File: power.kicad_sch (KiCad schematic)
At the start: 11 parts

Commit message: Finished circuit
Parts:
- added J4: 5V, symbol Connector:Conn_01x10_Pin
- added J5: GND, symbol Connector:Conn_01x10_Pin
- gave numbers to parts that had none: 11
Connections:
- net +5V: now also J4.1 (Pin_1), J4.10 (Pin_10), J4.2 (Pin_2), J4.3 (Pin_3), J4.4 (Pin_4), J4.5 (Pin_5), J4.6 (Pin_6), J4.7 (Pin_7), J4.8 (Pin_8), J4.9 (Pin_9)
- net GND: now also J3.2, J5.1 (Pin_1), J5.10 (Pin_10), J5.2 (Pin_2), J5.3 (Pin_3), J5.4 (Pin_4), J5.5 (Pin_5), J5.6 (Pin_6), J5.7 (Pin_7), J5.8 (Pin_8), J5.9 (Pin_9)

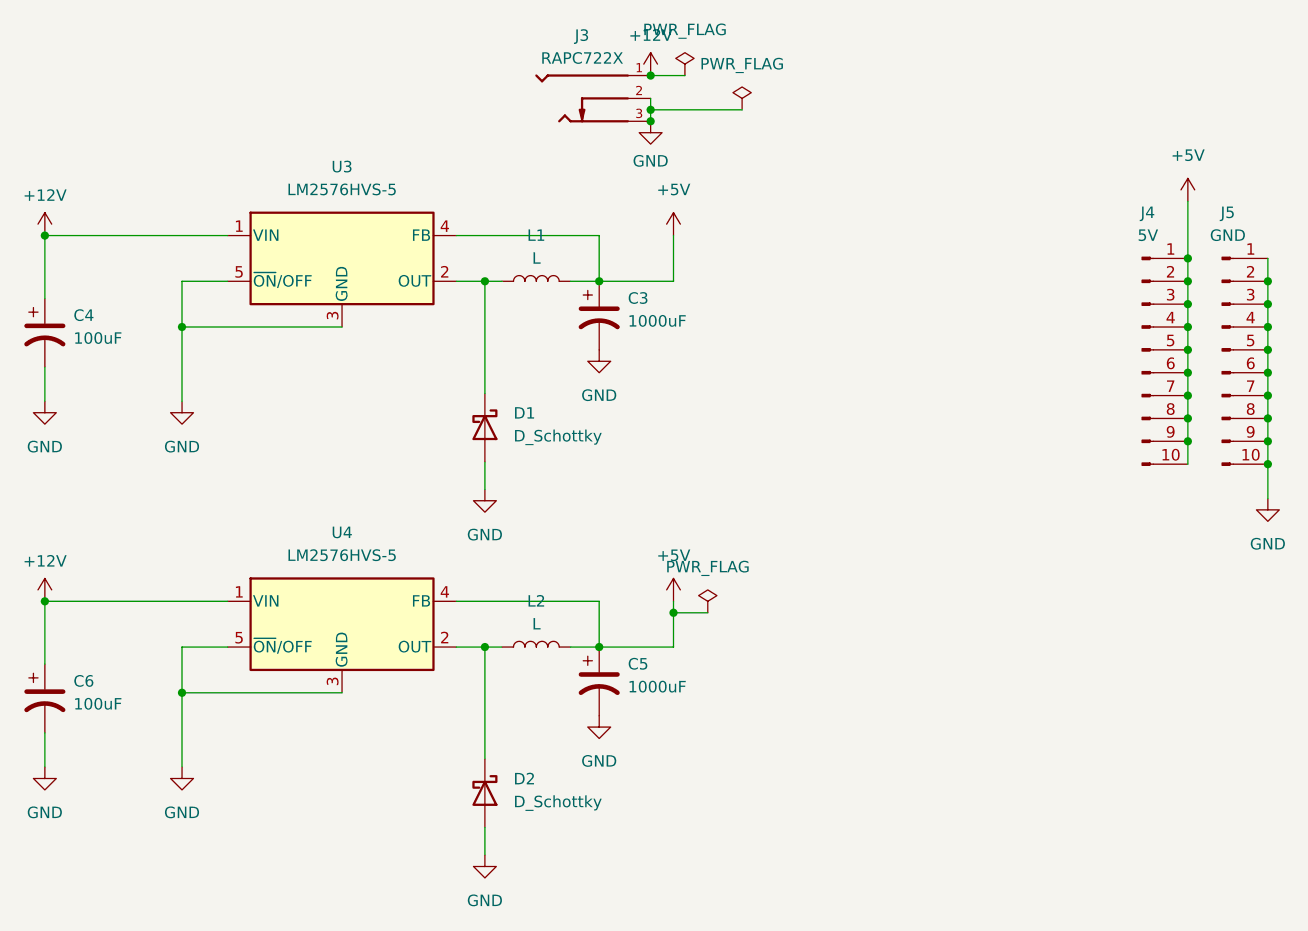
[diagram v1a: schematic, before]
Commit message: Updated the footprints for all the components.
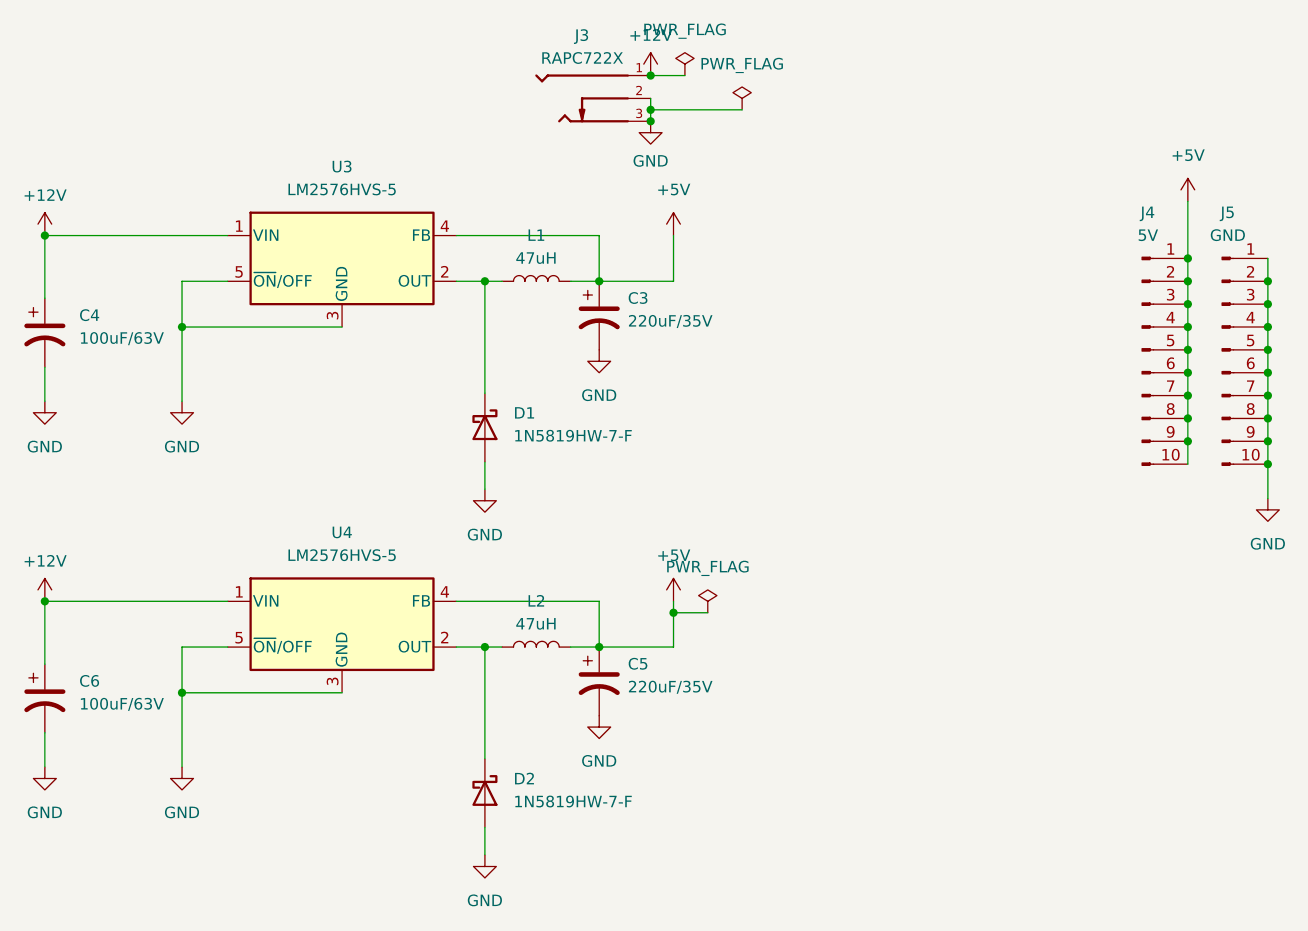
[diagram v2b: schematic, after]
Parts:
- C3, C5: value 1000uF -> 220uF/35V; footprint (none) -> Capacitor_SMD:CP_Elec_10x10; Field4 (none) -> EEH-ZA1V221P
- C4, C6: value 100uF -> 100uF/63V; footprint (none) -> Capacitor_SMD:CP_Elec_10x10; Field4 (none) -> UUX1J101MNL1GS
- D1, D2: value D_Schottky -> 1N5819HW-7-F; footprint (none) -> Diode_SMD:D_SOD-123
- J4, J5: footprint (none) -> Connector_PinSocket_2.54mm:PinSocket_2x05_P2.54mm_Vertical
- L1, L2: value L -> 47uH; footprint (none) -> Inductor_SMD:L_12x12mm_H8mm; Field4 (none) -> CDRH127/LDNP-470MC
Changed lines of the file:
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@@
       (effects (font (size 1.27 1.27)))
     )
-    (property "Value" "L" (at 82.55 90.17 90)
-      (effects (font (size 1.27 1.27)))
-    )
-    (property "Footprint" "" (at 82.55 92.71 0)
+    (property "Value" "47uH" (at 82.55 90.17 90)
+      (effects (font (size 1.27 1.27)))
+    )
+    (property "Footprint" "Inductor_SMD:L_12x12mm_H8mm" (at 82.55 92.71 0)
       (effects (font (size 1.27 1.27)) hide)
     )
     (property "Datasheet" "~" (at 82.55 92.71 0)
+      (effects (font (size 1.27 1.27)) hide)
+    )
+    (property "Field4" "CDRH127/LDNP-470MC" (at 82.55 92.71 90)
       (effects (font (size 1.27 1.27)) hide)
     )
@@
       (effects (font (size 1.27 1.27)))
     )
-    (property "Footprint" "" (at 158.75 59.69 0)
+    (property "Footprint" "Connector_PinSocket_2.54mm:PinSocket_2x05_P2.54mm_Vertical" (at 158.75 59.69 0)
       (effects (font (size 1.27 1.27)) hide)
     )
@@
       (effects (font (size 1.27 1.27)) (justify left))
     )
-    (property "Value" "D_Schottky" (at 80.01 69.2785 90)
-      (effects (font (size 1.27 1.27)) (justify left))
-    )
-    (property "Footprint" "" (at 76.835 68.326 0)
+    (property "Value" "1N5819HW-7-F" (at 80.01 69.2785 90)
+      (effects (font (size 1.27 1.27)) (justify left))
+    )
+    (property "Footprint" "Diode_SMD:D_SOD-123" (at 76.835 68.326 0)
       (effects (font (size 1.27 1.27)) hide)
     )
@@
   (symbol (lib_id "Device:C_Polarized_US") (at 27.94 98.425 0) (unit 1)
     (in_bom yes) (on_board yes) (dnp no) (fields_autoplaced)
-    (property "Reference" "C6" (at 31.115 96.52 0)
-      (effects (font (size 1.27 1.27)) (justify left))
-    )
-    (property "Value" "100uF" (at 31.115 99.06 0)
-      (effects (font (size 1.27 1.27)) (justify left))
-    )
-    (property "Footprint" "" (at 27.94 98.425 0)
+    (property "Reference" "C6" (at 31.75 96.52 0)
+      (effects (font (size 1.27 1.27)) (justify left))
+    )
+    (property "Value" "100uF/63V" (at 31.75 99.06 0)
+      (effects (font (size 1.27 1.27)) (justify left))
+    )
+    (property "Footprint" "Capacitor_SMD:CP_Elec_10x10" (at 27.94 98.425 0)
       (effects (font (size 1.27 1.27)) hide)
     )
@@
       (effects (font (size 1.27 1.27)) hide)
     )
+    (property "Field4" "UUX1J101MNL1GS" (at 27.94 98.425 0)
+      (effects (font (size 1.27 1.27)) hide)
+    )
     (pin "2")
     (pin "1")
@@
       (effects (font (size 1.27 1.27)) (justify left))
     )
-    (property "Value" "1000uF" (at 92.71 97.155 0)
-      (effects (font (size 1.27 1.27)) (justify left))
-    )
-    (property "Footprint" "" (at 89.535 96.52 0)
+    (property "Value" "220uF/35V" (at 92.71 97.155 0)
+      (effects (font (size 1.27 1.27)) (justify left))
+    )
+    (property "Footprint" "Capacitor_SMD:CP_Elec_10x10" (at 89.535 96.52 0)
       (effects (font (size 1.27 1.27)) hide)
     )
@@
       (effects (font (size 1.27 1.27)) hide)
     )
+    (property "Field4" "EEH-ZA1V221P" (at 89.535 96.52 0)
+      (effects (font (size 1.27 1.27)) hide)
+    )
     (pin "2")
     (pin "1")
@@
       (effects (font (size 1.27 1.27)))
     )
-    (property "Footprint" "" (at 149.86 59.69 0)
+    (property "Footprint" "Connector_PinSocket_2.54mm:PinSocket_2x05_P2.54mm_Vertical" (at 149.86 59.69 0)
       (effects (font (size 1.27 1.27)) hide)
     )
@@
       (effects (font (size 1.27 1.27)))
     )
-    (property "Value" "L" (at 82.55 49.53 90)
-      (effects (font (size 1.27 1.27)))
-    )
-    (property "Footprint" "" (at 82.55 52.07 0)
+    (property "Value" "47uH" (at 82.55 49.53 90)
+      (effects (font (size 1.27 1.27)))
+    )
+    (property "Footprint" "Inductor_SMD:L_12x12mm_H8mm" (at 82.55 52.07 0)
       (effects (font (size 1.27 1.27)) hide)
     )
@@
       (effects (font (size 1.27 1.27)) hide)
     )
+    (property "Field4" "CDRH127/LDNP-470MC" (at 82.55 52.07 90)
+      (effects (font (size 1.27 1.27)) hide)
+    )
     (pin "1")
     (pin "2")
@@
       (effects (font (size 1.27 1.27)) (justify left))
     )
-    (property "Value" "1000uF" (at 92.71 56.515 0)
-      (effects (font (size 1.27 1.27)) (justify left))
-    )
-    (property "Footprint" "" (at 89.535 55.88 0)
+    (property "Value" "220uF/35V" (at 92.71 56.515 0)
+      (effects (font (size 1.27 1.27)) (justify left))
+    )
+    (property "Footprint" "Capacitor_SMD:CP_Elec_10x10" (at 89.535 55.88 0)
       (effects (font (size 1.27 1.27)) hide)
     )
@@
       (effects (font (size 1.27 1.27)) hide)
     )
+    (property "Field4" "EEH-ZA1V221P" (at 89.535 55.88 0)
+      (effects (font (size 1.27 1.27)) hide)
+    )
     (pin "2")
     (pin "1")
@@
   (symbol (lib_id "Device:C_Polarized_US") (at 27.94 57.785 0) (unit 1)
     (in_bom yes) (on_board yes) (dnp no) (fields_autoplaced)
-    (property "Reference" "C4" (at 31.115 55.88 0)
-      (effects (font (size 1.27 1.27)) (justify left))
-    )
-    (property "Value" "100uF" (at 31.115 58.42 0)
-      (effects (font (size 1.27 1.27)) (justify left))
-    )
-    (property "Footprint" "" (at 27.94 57.785 0)
+    (property "Reference" "C4" (at 31.75 55.88 0)
+      (effects (font (size 1.27 1.27)) (justify left))
+    )
+    (property "Value" "100uF/63V" (at 31.75 58.42 0)
+      (effects (font (size 1.27 1.27)) (justify left))
+    )
+    (property "Footprint" "Capacitor_SMD:CP_Elec_10x10" (at 27.94 57.785 0)
       (effects (font (size 1.27 1.27)) hide)
     )
@@
       (effects (font (size 1.27 1.27)) hide)
     )
+    (property "Field4" "UUX1J101MNL1GS" (at 27.94 57.785 0)
+      (effects (font (size 1.27 1.27)) hide)
+    )
     (pin "2")
     (pin "1")
@@
       (effects (font (size 1.27 1.27)) (justify left))
     )
-    (property "Value" "D_Schottky" (at 80.01 109.9185 90)
-      (effects (font (size 1.27 1.27)) (justify left))
-    )
-    (property "Footprint" "" (at 76.835 108.966 0)
-      (effects (font (size 1.27 1.27)) hide)
-    )
+    (property "Value" "1N5819HW-7-F" (at 80.01 109.9185 90)
+      (effects (font (size 1.27 1.27)) (justify left))
+    )
+    (property "Footprint" "Diode_SMD:D_SOD-123" (at 76.835 108.966 0)
+      (effects (font (size 1.27 1.27)) hide)
+    )

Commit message: PCB Layout done
Routing yet to do.
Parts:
- J3: footprint RAPC722X:SWITCHCRAFT_RAPC722X -> Downloaded_footprints:SWITCHCRAFT_RAPC722X
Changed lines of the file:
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@@
       (effects (font (size 1.27 1.27)))
     )
-    (property "Footprint" "RAPC722X:SWITCHCRAFT_RAPC722X" (at 87.63 31.75 0)
+    (property "Footprint" "Downloaded_footprints:SWITCHCRAFT_RAPC722X" (at 87.63 31.75 0)
       (effects (font (size 1.27 1.27)) (justify bottom) hide)
     )
